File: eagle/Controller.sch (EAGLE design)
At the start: 43 parts, among them Q1 IRF530N, Q2 IRF530N, Q3 IRF530N, Q4 IRF530N, Q5 IRF530N, Q6 IRF530N, U1 BC337

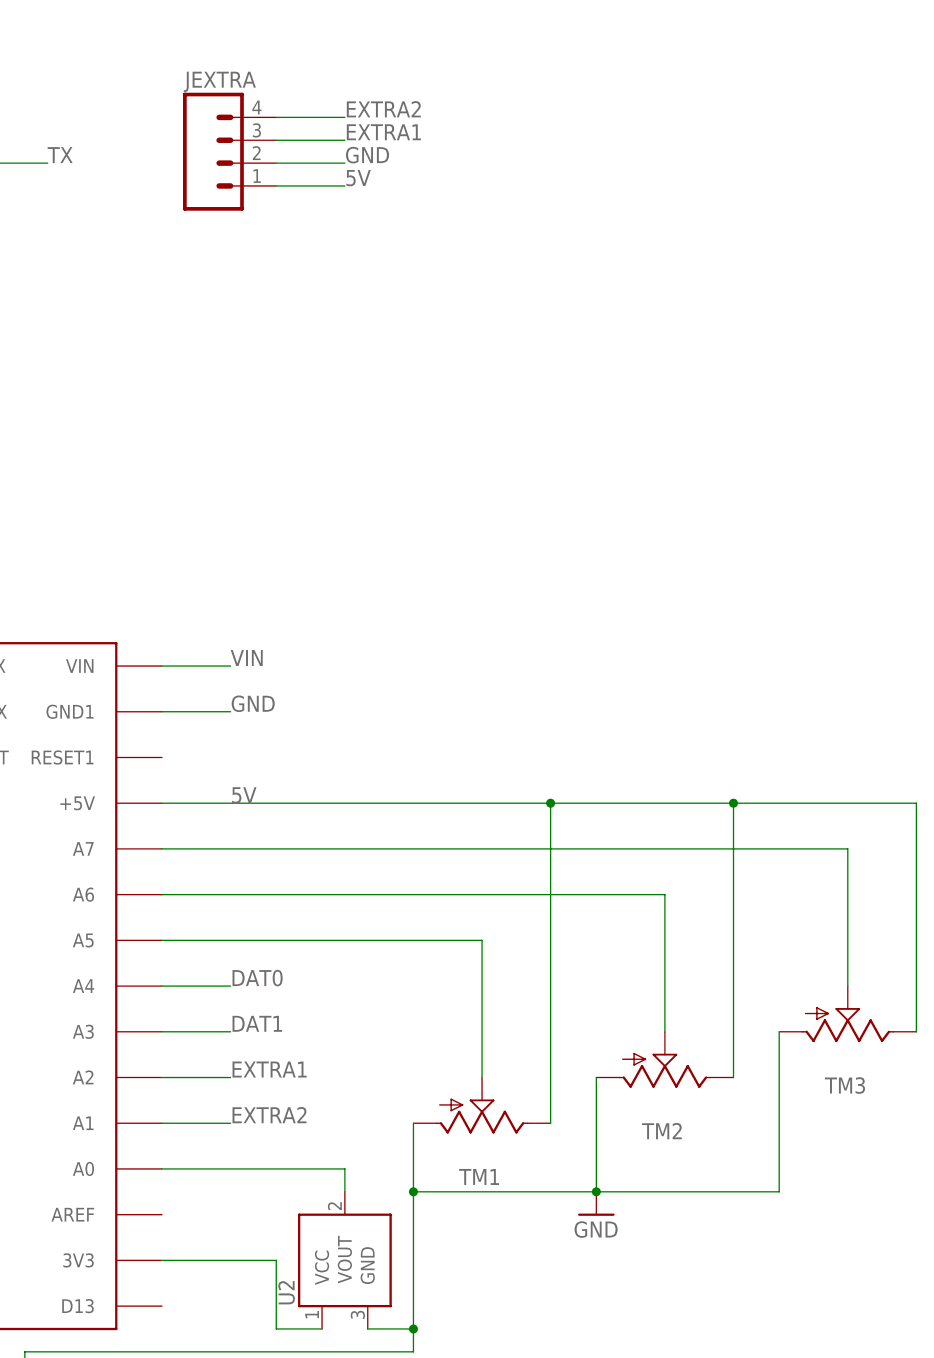
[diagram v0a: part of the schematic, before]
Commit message: Update board
Remove 2 trim pots and replace with EXTRA2/3
Increase size of vias
Increase border of board
Improve labeling
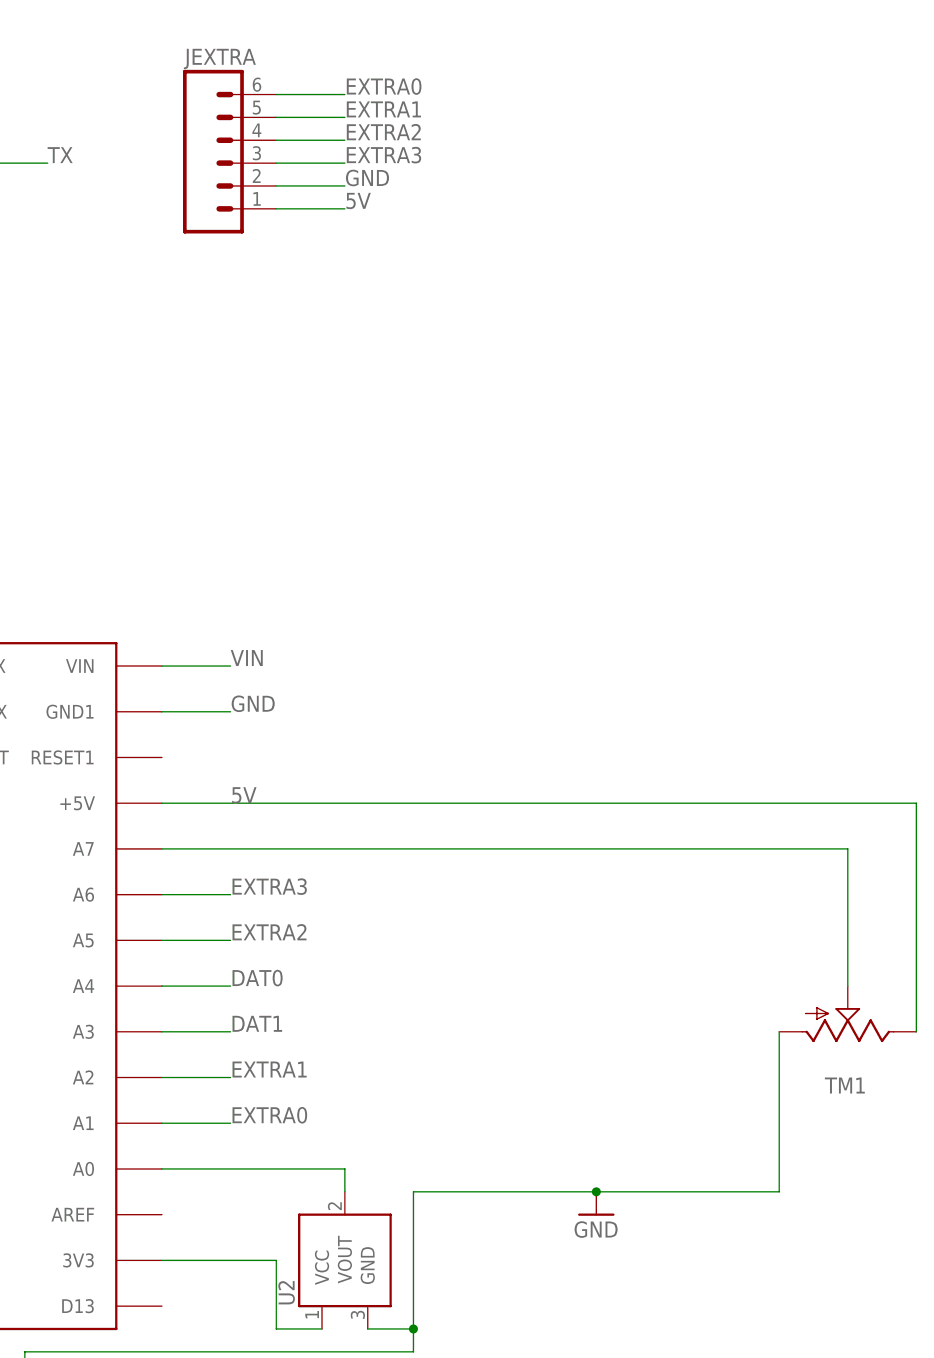
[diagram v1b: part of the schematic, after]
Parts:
- removed TM2, TM3: (no value), adafruit:TRIM
- JEXTRA: device SparkFun-Connectors:M04PTH -> SparkFun-Connectors:M06SILK_FEMALE_PTH
- NANO: value ARDUINONANO -> ARDUINONANONO-MOUNT; device jet-lib:ARDUINONANO -> jet-lib:ARDUINONANONO-MOUNT
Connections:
- removed net N$2: NANO.A6, TM2.S
- removed net N$3: NANO.A5, TM1.S
- new net EXTRA0: JEXTRA.6, NANO.A1
- new net EXTRA3: JEXTRA.3, NANO.A6
- net 5V: no longer TM2.E, TM3.E
- net EXTRA1: now also JEXTRA.5; no longer JEXTRA.3
- net EXTRA2: now also NANO.A5; no longer NANO.A1
- net GND: no longer TM2.A, TM3.A
- net N$1: now also TM1.S; no longer TM3.S
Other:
- moved on the sheet: TM1
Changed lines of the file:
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@@
 </classes>
 <parts>
-<part name="NANO" library="jet-lib" deviceset="ARDUINONANO" device="" value="ARDUINONANO"/>
+<part name="NANO" library="jet-lib" deviceset="ARDUINONANO" device="NO-MOUNT" value=""/>
 <part name="JRF" library="SparkFun-Connectors" deviceset="M07" device=""/>
 <part name="TM1" library="adafruit" deviceset="TRIM" device=""/>
-<part name="TM2" library="adafruit" deviceset="TRIM" device=""/>
-<part name="TM3" library="adafruit" deviceset="TRIM" device=""/>
 <part name="GND1" library="SparkFun-Aesthetics" deviceset="GND" device=""/>
 <part name="JPOW" library="SparkFun-Connectors" deviceset="M02" device="5MM"/>
@@
 <part name="RP12" library="SparkFun-Passives" deviceset="RESISTOR" device="PTH-1/4W" value="10k"/>
 <part name="U2" library="SparkFun-Sensors" deviceset="TMP36" device="GT9"/>
-<part name="JEXTRA" library="SparkFun-Connectors" deviceset="M04" device="PTH"/>
+<part name="JEXTRA" library="SparkFun-Connectors" deviceset="M06" device="SILK_FEMALE_PTH"/>
 <part name="R4" library="SparkFun-Passives" deviceset="RESISTOR" device="PTH-1/4W" value="3k"/>
 <part name="D1" library="SparkFun-LED" deviceset="LED" device="5MM" value="Red"/>
@@
 <instance part="NANO" gate="G$1" x="27.94" y="83.82"/>
 <instance part="JRF" gate="G$1" x="-116.84" y="114.3"/>
-<instance part="TM1" gate="G$1" x="88.9" y="30.48" rot="MR90"/>
-<instance part="TM2" gate="G$1" x="109.22" y="35.56" rot="MR90"/>
-<instance part="TM3" gate="G$1" x="129.54" y="40.64" rot="MR90"/>
+<instance part="TM1" gate="G$1" x="129.54" y="40.64" rot="MR90"/>
 <instance part="GND1" gate="1" x="101.6" y="20.32"/>
 <instance part="JPOW" gate="G$1" x="-119.38" y="144.78"/>
@@
 <pinref part="NANO" gate="G$1" pin="+5V"/>
 <label x="60.96" y="66.04" size="1.778" layer="95"/>
+<wire x1="53.34" y1="66.04" x2="137.16" y2="66.04" width="0.1524" layer="91"/>
 <pinref part="TM1" gate="G$1" pin="E"/>
-<wire x1="53.34" y1="66.04" x2="96.52" y2="66.04" width="0.1524" layer="91"/>
-<wire x1="96.52" y1="66.04" x2="96.52" y2="30.48" width="0.1524" layer="91"/>
-<pinref part="TM2" gate="G$1" pin="E"/>
-<wire x1="96.52" y1="66.04" x2="116.84" y2="66.04" width="0.1524" layer="91"/>
-<wire x1="116.84" y1="66.04" x2="116.84" y2="35.56" width="0.1524" layer="91"/>
-<junction x="96.52" y="66.04"/>
-<pinref part="TM3" gate="G$1" pin="E"/>
-<wire x1="116.84" y1="66.04" x2="137.16" y2="66.04" width="0.1524" layer="91"/>
 <wire x1="137.16" y1="66.04" x2="137.16" y2="40.64" width="0.1524" layer="91"/>
-<junction x="116.84" y="66.04"/>
 </segment>
 <segment>
 <pinref part="JEXTRA" gate="G$1" pin="1"/>
-<wire x1="66.04" y1="134.62" x2="73.66" y2="134.62" width="0.1524" layer="91"/>
-<label x="73.66" y="134.62" size="1.778" layer="95"/>
+<wire x1="66.04" y1="132.08" x2="73.66" y2="132.08" width="0.1524" layer="91"/>
+<label x="73.66" y="132.08" size="1.778" layer="95"/>
 </segment>
 </net>
 <net name="GND" class="0">
 <segment>
+<wire x1="81.28" y1="22.86" x2="101.6" y2="22.86" width="0.1524" layer="91"/>
 <pinref part="TM1" gate="G$1" pin="A"/>
-<wire x1="81.28" y1="30.48" x2="81.28" y2="22.86" width="0.1524" layer="91"/>
-<pinref part="TM2" gate="G$1" pin="A"/>
-<wire x1="81.28" y1="22.86" x2="101.6" y2="22.86" width="0.1524" layer="91"/>
-<wire x1="101.6" y1="22.86" x2="101.6" y2="35.56" width="0.1524" layer="91"/>
-<pinref part="TM3" gate="G$1" pin="A"/>
 <wire x1="101.6" y1="22.86" x2="121.92" y2="22.86" width="0.1524" layer="91"/>
 <wire x1="121.92" y1="22.86" x2="121.92" y2="40.64" width="0.1524" layer="91"/>
@@
 <wire x1="76.2" y1="7.62" x2="81.28" y2="7.62" width="0.1524" layer="91"/>
 <wire x1="81.28" y1="7.62" x2="81.28" y2="22.86" width="0.1524" layer="91"/>
-<junction x="81.28" y="22.86"/>
 <pinref part="D1" gate="G$1" pin="C"/>
 <wire x1="12.7" y1="-10.16" x2="38.1" y2="-10.16" width="0.1524" layer="91"/>
@@
 <segment>
 <pinref part="JEXTRA" gate="G$1" pin="2"/>
-<wire x1="66.04" y1="137.16" x2="73.66" y2="137.16" width="0.1524" layer="91"/>
-<label x="73.66" y="137.16" size="1.778" layer="95"/>
+<wire x1="66.04" y1="134.62" x2="73.66" y2="134.62" width="0.1524" layer="91"/>
+<label x="73.66" y="134.62" size="1.778" layer="95"/>
 </segment>
 </net>
@@
 <net name="EXTRA2" class="0">
 <segment>
-<pinref part="NANO" gate="G$1" pin="A1"/>
-<wire x1="53.34" y1="30.48" x2="60.96" y2="30.48" width="0.1524" layer="91"/>
-<label x="60.96" y="30.48" size="1.778" layer="95"/>
-</segment>
-<segment>
 <pinref part="JEXTRA" gate="G$1" pin="4"/>
-<wire x1="66.04" y1="142.24" x2="73.66" y2="142.24" width="0.1524" layer="91"/>
-<label x="73.66" y="142.24" size="1.778" layer="95"/>
-</segment>
-</net>
-<net name="N$1" class="0">
-<segment>
-<pinref part="TM3" gate="G$1" pin="S"/>
-<pinref part="NANO" gate="G$1" pin="A7"/>
-<wire x1="53.34" y1="60.96" x2="129.54" y2="60.96" width="0.1524" layer="91"/>
-<wire x1="129.54" y1="60.96" x2="129.54" y2="45.72" width="0.1524" layer="91"/>
-</segment>
-</net>
-<net name="N$2" class="0">
-<segment>
-<pinref part="TM2" gate="G$1" pin="S"/>
-<pinref part="NANO" gate="G$1" pin="A6"/>
-<wire x1="53.34" y1="55.88" x2="109.22" y2="55.88" width="0.1524" layer="91"/>
-<wire x1="109.22" y1="55.88" x2="109.22" y2="40.64" width="0.1524" layer="91"/>
-</segment>
-</net>
-<net name="N$3" class="0">
-<segment>
-<pinref part="TM1" gate="G$1" pin="S"/>
+<wire x1="66.04" y1="139.7" x2="73.66" y2="139.7" width="0.1524" layer="91"/>
+<label x="73.66" y="139.7" size="1.778" layer="95"/>
+</segment>
+<segment>
 <pinref part="NANO" gate="G$1" pin="A5"/>
-<wire x1="53.34" y1="50.8" x2="88.9" y2="50.8" width="0.1524" layer="91"/>
-<wire x1="88.9" y1="50.8" x2="88.9" y2="35.56" width="0.1524" layer="91"/>
+<wire x1="53.34" y1="50.8" x2="60.96" y2="50.8" width="0.1524" layer="91"/>
+<label x="60.96" y="50.8" size="1.778" layer="95"/>
 </segment>
 </net>
@@
 </segment>
 <segment>
-<pinref part="JEXTRA" gate="G$1" pin="3"/>
-<wire x1="66.04" y1="139.7" x2="73.66" y2="139.7" width="0.1524" layer="91"/>
-<label x="73.66" y="139.7" size="1.778" layer="95"/>
+<pinref part="JEXTRA" gate="G$1" pin="5"/>
+<wire x1="66.04" y1="142.24" x2="73.66" y2="142.24" width="0.1524" layer="91"/>
+<label x="73.66" y="142.24" size="1.778" layer="95"/>
 </segment>
 </net>
@@
 </segment>
 </net>
+<net name="N$1" class="0">
+<segment>
+<pinref part="NANO" gate="G$1" pin="A7"/>
+<pinref part="TM1" gate="G$1" pin="S"/>
+<wire x1="53.34" y1="60.96" x2="129.54" y2="60.96" width="0.1524" layer="91"/>
+<wire x1="129.54" y1="60.96" x2="129.54" y2="45.72" width="0.1524" layer="91"/>
+</segment>
+</net>
+<net name="EXTRA3" class="0">
+<segment>
+<pinref part="NANO" gate="G$1" pin="A6"/>
+<wire x1="53.34" y1="55.88" x2="60.96" y2="55.88" width="0.1524" layer="91"/>
+<label x="60.96" y="55.88" size="1.778" layer="95"/>
+</segment>
+<segment>
+<pinref part="JEXTRA" gate="G$1" pin="3"/>
+<wire x1="66.04" y1="137.16" x2="73.66" y2="137.16" width="0.1524" layer="91"/>
+<label x="73.66" y="137.16" size="1.778" layer="95"/>
+</segment>
+</net>
+<net name="EXTRA0" class="0">
+<segment>
+<pinref part="NANO" gate="G$1" pin="A1"/>
+<wire x1="53.34" y1="30.48" x2="60.96" y2="30.48" width="0.1524" layer="91"/>
+<label x="60.96" y="30.48" size="1.778" layer="95"/>
+</segment>
+<segment>
+<pinref part="JEXTRA" gate="G$1" pin="6"/>
+<wire x1="66.04" y1="144.78" x2="73.66" y2="144.78" width="0.1524" layer="91"/>
+<label x="73.66" y="144.78" size="1.778" layer="95"/>
+</segment>
+</net>

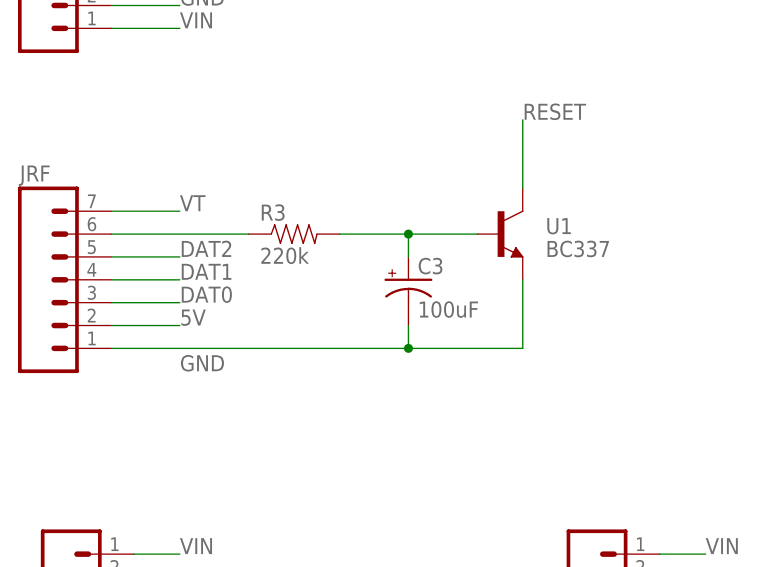
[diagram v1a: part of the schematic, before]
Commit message: Change reset circuit to work with lower Arduino resistor values
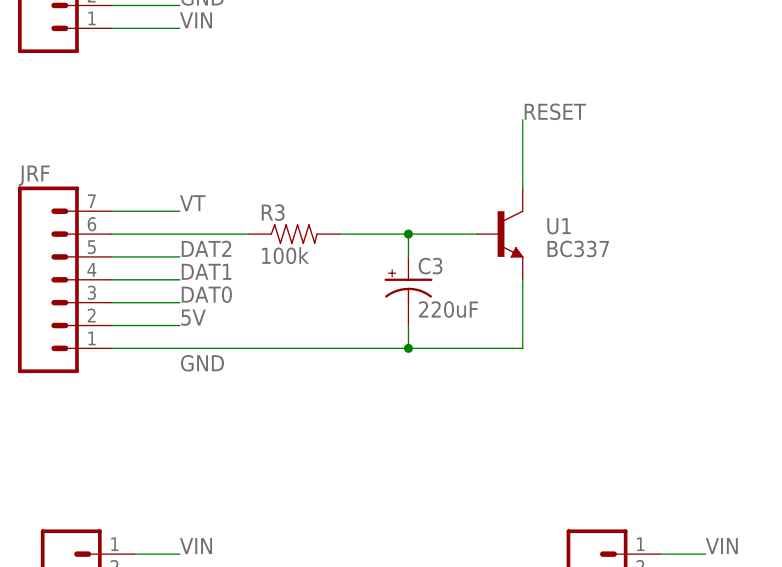
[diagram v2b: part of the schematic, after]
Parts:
- C3: value 100uF -> 220uF
- R3: value 220k -> 100k
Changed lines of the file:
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@@
 <grid distance="0.1" unitdist="inch" unit="inch" style="lines" multiple="1" display="no" altdistance="0.01" altunitdist="inch" altunit="inch"/>
 <layers>
-<layer number="1" name="Top" color="4" fill="1" visible="yes" active="no"/>
-<layer number="16" name="Bottom" color="1" fill="1" visible="yes" active="no"/>
-<layer number="17" name="Pads" color="2" fill="1" visible="yes" active="no"/>
-<layer number="18" name="Vias" color="2" fill="1" visible="yes" active="no"/>
-<layer number="19" name="Unrouted" color="6" fill="1" visible="yes" active="no"/>
-<layer number="20" name="Dimension" color="15" fill="1" visible="yes" active="no"/>
-<layer number="21" name="tPlace" color="7" fill="1" visible="yes" active="no"/>
-<layer number="22" name="bPlace" color="7" fill="1" visible="yes" active="no"/>
-<layer number="23" name="tOrigins" color="15" fill="1" visible="yes" active="no"/>
-<layer number="24" name="bOrigins" color="15" fill="1" visible="yes" active="no"/>
-<layer number="25" name="tNames" color="7" fill="1" visible="yes" active="no"/>
-<layer number="26" name="bNames" color="7" fill="1" visible="yes" active="no"/>
-<layer number="27" name="tValues" color="7" fill="1" visible="yes" active="no"/>
-<layer number="28" name="bValues" color="7" fill="1" visible="yes" active="no"/>
+<layer number="1" name="Top" color="4" fill="1" visible="no" active="no"/>
+<layer number="16" name="Bottom" color="1" fill="1" visible="no" active="no"/>
+<layer number="17" name="Pads" color="2" fill="1" visible="no" active="no"/>
+<layer number="18" name="Vias" color="2" fill="1" visible="no" active="no"/>
+<layer number="19" name="Unrouted" color="6" fill="1" visible="no" active="no"/>
+<layer number="20" name="Dimension" color="15" fill="1" visible="no" active="no"/>
+<layer number="21" name="tPlace" color="7" fill="1" visible="no" active="no"/>
+<layer number="22" name="bPlace" color="7" fill="1" visible="no" active="no"/>
+<layer number="23" name="tOrigins" color="15" fill="1" visible="no" active="no"/>
+<layer number="24" name="bOrigins" color="15" fill="1" visible="no" active="no"/>
+<layer number="25" name="tNames" color="7" fill="1" visible="no" active="no"/>
+<layer number="26" name="bNames" color="7" fill="1" visible="no" active="no"/>
+<layer number="27" name="tValues" color="7" fill="1" visible="no" active="no"/>
+<layer number="28" name="bValues" color="7" fill="1" visible="no" active="no"/>
 <layer number="29" name="tStop" color="7" fill="3" visible="no" active="no"/>
 <layer number="30" name="bStop" color="7" fill="6" visible="no" active="no"/>
@@
 <layer number="35" name="tGlue" color="7" fill="4" visible="no" active="no"/>
 <layer number="36" name="bGlue" color="7" fill="5" visible="no" active="no"/>
-<layer number="37" name="tTest" color="7" fill="1" visible="yes" active="no"/>
-<layer number="38" name="bTest" color="7" fill="1" visible="yes" active="no"/>
+<layer number="37" name="tTest" color="7" fill="1" visible="no" active="no"/>
+<layer number="38" name="bTest" color="7" fill="1" visible="no" active="no"/>
 <layer number="39" name="tKeepout" color="4" fill="11" visible="no" active="no"/>
 <layer number="40" name="bKeepout" color="1" fill="11" visible="no" active="no"/>
@@
 <layer number="44" name="Drills" color="7" fill="1" visible="no" active="no"/>
 <layer number="45" name="Holes" color="7" fill="1" visible="no" active="no"/>
-<layer number="46" name="Milling" color="3" fill="1" visible="yes" active="no"/>
-<layer number="47" name="Measures" color="7" fill="1" visible="yes" active="no"/>
-<layer number="48" name="Document" color="7" fill="1" visible="yes" active="no"/>
-<layer number="49" name="Reference" color="7" fill="1" visible="yes" active="no"/>
-<layer number="50" name="dxf" color="7" fill="1" visible="yes" active="no"/>
-<layer number="51" name="tDocu" color="7" fill="1" visible="yes" active="no"/>
-<layer number="52" name="bDocu" color="7" fill="1" visible="yes" active="no"/>
-<layer number="53" name="tGND_GNDA" color="7" fill="9" visible="yes" active="no"/>
-<layer number="54" name="bGND_GNDA" color="1" fill="9" visible="yes" active="no"/>
-<layer number="56" name="wert" color="7" fill="1" visible="yes" active="no"/>
-<layer number="57" name="tCAD" color="7" fill="1" visible="yes" active="no"/>
-<layer number="59" name="tCarbon" color="7" fill="1" visible="yes" active="no"/>
-<layer number="60" name="bCarbon" color="7" fill="1" visible="yes" active="no"/>
+<layer number="46" name="Milling" color="3" fill="1" visible="no" active="no"/>
+<layer number="47" name="Measures" color="7" fill="1" visible="no" active="no"/>
+<layer number="48" name="Document" color="7" fill="1" visible="no" active="no"/>
+<layer number="49" name="Reference" color="7" fill="1" visible="no" active="no"/>
+<layer number="50" name="dxf" color="7" fill="1" visible="no" active="no"/>
+<layer number="51" name="tDocu" color="7" fill="1" visible="no" active="no"/>
+<layer number="52" name="bDocu" color="7" fill="1" visible="no" active="no"/>
+<layer number="53" name="tGND_GNDA" color="7" fill="9" visible="no" active="no"/>
+<layer number="54" name="bGND_GNDA" color="1" fill="9" visible="no" active="no"/>
+<layer number="56" name="wert" color="7" fill="1" visible="no" active="no"/>
+<layer number="57" name="tCAD" color="7" fill="1" visible="no" active="no"/>
+<layer number="59" name="tCarbon" color="7" fill="1" visible="no" active="no"/>
+<layer number="60" name="bCarbon" color="7" fill="1" visible="no" active="no"/>
 <layer number="90" name="Modules" color="5" fill="1" visible="yes" active="yes"/>
 <layer number="91" name="Nets" color="2" fill="1" visible="yes" active="yes"/>
@@
 <attributes>
 <attribute name="CNAME" value="Mooring Lights Controller"/>
-<attribute name="CREVISION" value="0.1"/>
+<attribute name="CREVISION" value="0.1.1"/>
 <attribute name="DESIGNER" value="John Bayly"/>
 </attributes>
@@
 <part name="C2" library="SparkFun-Capacitors" deviceset="10UF-25V-20%(PTH)" device="" value="10uF"/>
 <part name="JWIFI" library="SparkFun-Connectors" deviceset="M04" device="PTH"/>
-<part name="R3" library="SparkFun-Passives" deviceset="RESISTOR" device="PTH-1/4W" value="220k"/>
-<part name="C3" library="SparkFun-Capacitors" deviceset="100UF-25V-20%(PTH)" device="" value="100uF"/>
+<part name="R3" library="SparkFun-Passives" deviceset="RESISTOR" device="PTH-1/4W" value="100k"/>
+<part name="C3" library="SparkFun-Capacitors" deviceset="100UF-25V-20%(PTH)" device="" value="220uF"/>
 <part name="JPWM1" library="SparkFun-Connectors" deviceset="M02" device="5MM"/>
 <part name="RP1" library="SparkFun-Passives" deviceset="RESISTOR" device="PTH-1/4W" value="100"/>
